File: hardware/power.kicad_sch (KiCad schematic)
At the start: 21 parts, among them J1 Conn_01x03_Pin, Q1 SI2301CDS-T1-GE3, U1 TMA-1212D, U2 TPS54302

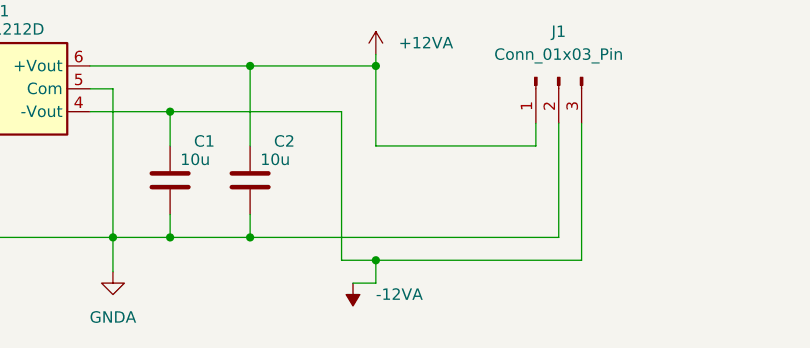
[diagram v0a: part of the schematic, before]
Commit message: cleanup - remove unused schematics
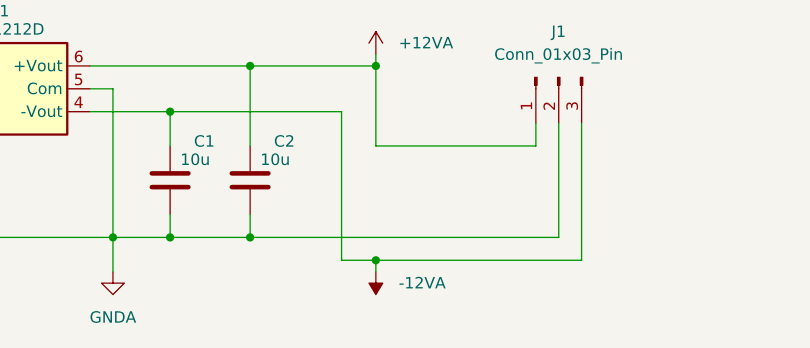
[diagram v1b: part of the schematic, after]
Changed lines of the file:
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@@
-	(wire
-		(pts
-			(xy 102.87 152.4) (xy 100.33 152.4)
-		)
-		(stroke
-			(width 0)
-			(type default)
-		)
-	)
 	(wire
 		(pts
@@
 	(wire
 		(pts
-			(xy 102.87 149.86) (xy 102.87 152.4)
+			(xy 102.87 149.86) (xy 102.87 151.13)
 		)
 		(stroke
@@
 		(dnp no)
 		(fields_autoplaced yes)
-		(property "Reference" "#PWR04"
+		(property "Reference" "#PWR03"
 			(at 102.87 130.81 0)
 			(effects
@@
 			(project "triptech"
 				(path "/55cca6a8-30da-4c13-b2f2-a01401e2b54c/a1b2c3d4-1111-4000-8000-000000000001"
-					(reference "#PWR04")
+					(reference "#PWR03")
 					(unit 1)
 				)
@@
 	(symbol
 		(lib_id "power:-12VA")
-		(at 100.33 152.4 180)
+		(at 102.87 151.13 180)
 		(unit 1)
 		(exclude_from_sim no)
@@
 		(dnp no)
 		(fields_autoplaced yes)
-		(property "Reference" "#PWR03"
-			(at 100.33 148.59 0)
+		(property "Reference" "#PWR04"
+			(at 102.87 147.32 0)
 			(effects
 				(font
@@
 		)
 		(property "Value" "-12VA"
-			(at 102.87 153.6699 0)
+			(at 105.41 152.3999 0)
 			(effects
 				(font
@@
 		)
 		(property "Footprint" ""
-			(at 100.33 152.4 0)
+			(at 102.87 151.13 0)
 			(effects
 				(font
@@
 		)
 		(property "Datasheet" ""
-			(at 100.33 152.4 0)
+			(at 102.87 151.13 0)
 			(effects
 				(font
@@
 		)
 		(property "Description" "Power symbol creates a global label with name \"-12VA\""
-			(at 100.33 152.4 0)
+			(at 102.87 151.13 0)
 			(effects
 				(font
@@
 			(project "triptech"
 				(path "/55cca6a8-30da-4c13-b2f2-a01401e2b54c/a1b2c3d4-1111-4000-8000-000000000001"
-					(reference "#PWR03")
-					(unit 1)
-				)
+					(reference "#PWR04")
+					(unit 1)
+				)

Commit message: PCB Assembledish Design checks next
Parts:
- added L1, L2: BLM18PG121SN1, Inductor_SMD:L_0603_1608Metric, symbol Device:L
- C4: symbol Device:CP -> Device:C_Polarized
- J1: value Conn_01x03_Pin -> Power; footprint Connector_PinHeader_2.54mm:PinHeader_1x03_P2.54mm_Vertical -> Connector_PinHeader_2.54mm:PinHeader_2x04_P2.54mm_Vertical; symbol Connector:Conn_01x03_Pin -> Connector_Generic:Conn_02x04_Odd_Even
- renumbered L1 to L3
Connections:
- net +12VA: now also J1.2 (Pin_2), L2.2; no longer C2.1, J1.1 (Pin_1), U1.6 (+Vout)
- net +5V: now also J1.1 (Pin_1)
- net -12VA: now also J1.6 (Pin_6), L1.2; no longer C1.1, J1.3 (Pin_3), U1.4 (-Vout)
- net GND: now also C1.2, C2.2, J1.3 (Pin_3), J1.4 (Pin_4), J1.5 (Pin_5), U1.2 (-Vin), U1.5 (Com)
- removed net GNDA: C1.2, C2.2, J1.2 (Pin_2), U1.2 (-Vin), U1.5 (Com)
- new net: C2.1, L2.1, U1.6 (+Vout)
- new net: C1.1, L1.1, U1.4 (-Vout)
- new net +3V3A: J1.8 (Pin_8)
- new net +3V3D: J1.7 (Pin_7)
- no-connect marks 0 -> 1
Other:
- moved on the sheet: C3
